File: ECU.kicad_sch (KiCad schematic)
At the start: 2 parts

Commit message: Create new top level
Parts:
- U?: value AEM_Infinity_5_Pin41-80 -> (none)
- U?: value AEM_Infinity_5_Pin1-40 -> (none)
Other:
- removed sheet Engine Overview
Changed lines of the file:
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@@
       (effects (font (size 1.27 1.27)) (justify left))
     )
-    (property "Value" "AEM_Infinity_5_Pin41-80" (id 1) (at 123.952 177.292 0)
+    (property "Value" "" (id 1) (at 123.952 177.292 0)
       (effects (font (size 1.27 1.27)) (justify left))
     )
@@
       (effects (font (size 1.27 1.27)) (justify left))
     )
-    (property "Value" "AEM_Infinity_5_Pin1-40" (id 1) (at 72.136 177.038 0)
+    (property "Value" "" (id 1) (at 72.136 177.038 0)
       (effects (font (size 1.27 1.27)) (justify left))
     )
@@
     )
   )
-  (sheet (at 246.38 25.4) (size 19.812 12.954) (fields_autoplaced)
-    (stroke (width 0.1524) (type solid) (color 0 0 0 0))
-    (fill (color 0 0 0 0.0000))
-    (property "Sheet name" "Engine Overview" (id 0) (at 246.38 24.6884 0)
-      (effects (font (size 1.27 1.27)) (justify left bottom))
-    )
-    (property "Sheet file" "Engine.kicad_sch" (id 1) (at 246.38 38.9386 0)
-      (effects (font (size 1.27 1.27)) (justify left top))
-    )
-  )

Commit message: HUGE TOP LEVEL
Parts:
- U?: value (none) -> AEM_Infinity_5_Pin41-80
- U?: value (none) -> AEM_Infinity_5_Pin1-40
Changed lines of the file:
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@@
       (effects (font (size 1.27 1.27)) (justify left))
     )
-    (property "Value" "" (id 1) (at 123.952 177.292 0)
+    (property "Value" "AEM_Infinity_5_Pin41-80" (id 1) (at 123.952 177.292 0)
       (effects (font (size 1.27 1.27)) (justify left))
     )
@@
       (effects (font (size 1.27 1.27)) (justify left))
     )
-    (property "Value" "" (id 1) (at 72.136 177.038 0)
+    (property "Value" "AEM_Infinity_5_Pin1-40" (id 1) (at 72.136 177.038 0)
       (effects (font (size 1.27 1.27)) (justify left))
     )

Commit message: Filled in Many Sheets
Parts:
- removed U?: AEM_Infinity_5_Pin41-80, symbol SCR23 Library:AEM_Infinity_5_Pin41-80
- removed U?: AEM_Infinity_5_Pin1-40, symbol SCR23 Library:AEM_Infinity_5_Pin1-40
- added U?: ECU, symbol Ty lib:ECU
- added U?: AEM_Infinity_5_Pin41-80, symbol SCR23 Library:AEM_Infinity_5_Pin41-80
- added U?: DTM_12P_BROWN_FEMALE, symbol SCR23 Library:DTM04-12pb
- added U?: DTM_12P_GRAY_FEMALE, symbol SCR23 Library:DTM04-12pb
- added U?: DTM_12P_BLACK_FEMALE, symbol SCR23 Library:DTM04-12pb
- added U?: DTM_12P_GREEN_FEMALE, symbol SCR23 Library:DTM04-12pb
- added U?: DT_12P_BLACK_FEMALE, symbol SCR23 Library:DTM04-12pb
- added U?: DT_12P_GREEN_FEMALE, symbol SCR23 Library:DTM04-12pb
- added U?: AEM_Infinity_5_Pin1-40, symbol SCR23 Library:AEM_Infinity_5_Pin1-40
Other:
- removed sheet Charging System
- removed sheet Coil Overview
- removed sheet DTM Dash
- removed sheet ECU Main Loom
- added sheet ECU Pinout (ECU_Pinout.kicad_sch)
- note added: "Black DTM 12P to FUSEBOX"
- note added: "ECU"
- note added: "ECU to COIL DRIVER"
- note added: "ECU to FUSEBOX"
- note added: "ECU to INJECTOR"
- note added: "GOES TO DASHBOARD"

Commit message: Getting Ready for CDR
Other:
- added sheet Coil Driver (Coil_Driver.kicad_sch)
- note added: "ECU to ENGINE"
- note removed: "ECU to COIL DRIVER"
- note removed: "ECU to INJECTOR"
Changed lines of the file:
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@@
     (effects (font (size 1.27 1.27)) (justify left bottom))
   )
-  (text "ECU to COIL DRIVER" (at 244.602 76.2 0)
+  (text "ECU to ENGINE" (at 244.602 76.2 0)
     (effects (font (size 1.27 1.27)) (justify left bottom))
   )
@@
     (effects (font (size 1.27 1.27)) (justify left bottom))
   )
-  (text "ECU to INJECTOR" (at 207.264 76.962 0)
+  (text "ECU to ENGINE" (at 207.264 76.962 0)
     (effects (font (size 1.27 1.27)) (justify left bottom))
   )
@@
     (property "Intersheet References" "${INTERSHEET_REFS}" (id 0) (at 192.4008 29.1545 0)
       (effects (font (size 0.889 0.889)) (justify left) hide)
+    )
+  )
+  (global_label "GND" (shape input) (at 233.426 45.974 180) (fields_autoplaced)
+    (effects (font (size 0.889 0.889)) (justify right))
+    (property "Intersheet References" "${INTERSHEET_REFS}" (id 0) (at 229.0276 45.9185 0)
+      (effects (font (size 0.889 0.889)) (justify right) hide)
     )
   )
@@
     )
   )
+  (global_label "11 - Coil 4" (shape input) (at 233.426 43.942 180) (fields_autoplaced)
+    (effects (font (size 0.889 0.889)) (justify right))
+    (property "Intersheet References" "${INTERSHEET_REFS}" (id 0) (at 223.4819 43.8865 0)
+      (effects (font (size 0.889 0.889)) (justify right) hide)
+    )
+  )
   (global_label "Injection 2 - 77" (shape input) (at 179.324 27.178 0) (fields_autoplaced)
     (effects (font (size 0.889 0.889)) (justify left))
@@
     (property "Intersheet References" "${INTERSHEET_REFS}" (id 0) (at 145.6648 53.2845 0)
       (effects (font (size 0.889 0.889)) (justify left) hide)
+    )
+  )
+  (global_label "12 - Coil 3" (shape input) (at 233.426 41.91 180) (fields_autoplaced)
+    (effects (font (size 0.889 0.889)) (justify right))
+    (property "Intersheet References" "${INTERSHEET_REFS}" (id 0) (at 223.4819 41.8545 0)
+      (effects (font (size 0.889 0.889)) (justify right) hide)
     )
   )
@@
     )
   )
+  (global_label "13 - Coil 2" (shape input) (at 233.426 39.878 180) (fields_autoplaced)
+    (effects (font (size 0.889 0.889)) (justify right))
+    (property "Intersheet References" "${INTERSHEET_REFS}" (id 0) (at 223.4819 39.8225 0)
+      (effects (font (size 0.889 0.889)) (justify right) hide)
+    )
+  )
   (global_label "13 - Coil 2" (shape input) (at 106.68 35.052 180) (fields_autoplaced)
     (effects (font (size 0.889 0.889)) (justify right))
@@
     )
   )
+  (global_label "14 - Coil 1" (shape input) (at 233.426 37.846 180) (fields_autoplaced)
+    (effects (font (size 0.889 0.889)) (justify right))
+    (property "Intersheet References" "${INTERSHEET_REFS}" (id 0) (at 223.4819 37.7905 0)
+      (effects (font (size 0.889 0.889)) (justify right) hide)
+    )
+  )
   (global_label "Ground - 33" (shape input) (at 127 35.052 0) (fields_autoplaced)
     (effects (font (size 0.889 0.889)) (justify left))
@@
       (effects (font (size 0.889 0.889)) (justify left) hide)
     )
+  )
+  (hierarchical_label "COIL_SGN_4" (shape input) (at 233.426 37.846 0)
+    (effects (font (size 1.27 1.27)) (justify left))
+  )
+  (hierarchical_label "COIL_4" (shape output) (at 261.366 37.846 0)
+    (effects (font (size 1.27 1.27)) (justify left))
+  )
+  (hierarchical_label "COIL_GND" (shape input) (at 233.426 45.974 0)
+    (effects (font (size 1.27 1.27)) (justify left))
+  )
+  (hierarchical_label "COIL_SGN_3" (shape input) (at 233.426 39.878 0)
+    (effects (font (size 1.27 1.27)) (justify left))
+  )
+  (hierarchical_label "COIL_SGN_2" (shape input) (at 233.426 41.91 0)
+    (effects (font (size 1.27 1.27)) (justify left))
+  )
+  (hierarchical_label "COIL_2" (shape output) (at 261.366 41.91 0)
+    (effects (font (size 1.27 1.27)) (justify left))
+  )
+  (hierarchical_label "COIL_1" (shape output) (at 261.366 43.942 0)
+    (effects (font (size 1.27 1.27)) (justify left))
+  )
+  (hierarchical_label "COIL_3" (shape output) (at 261.366 39.878 0)
+    (effects (font (size 1.27 1.27)) (justify left))
+  )
+  (hierarchical_label "COIL_SGN_1" (shape input) (at 233.426 43.942 0)
+    (effects (font (size 1.27 1.27)) (justify left))
   )
   (symbol (lib_id "Ty lib:ECU") (at 49.022 166.37 0) (unit 1)
@@
       (effects (font (size 1.27 1.27)) (justify left top))
     )
+  )
+  (sheet (at 233.426 36.322) (size 27.94 10.922) (fields_autoplaced)
+    (stroke (width 0.1524) (type solid) (color 0 0 0 0))
+    (fill (color 0 0 0 0.0000))
+    (property "Sheet name" "Coil Driver" (id 0) (at 233.426 35.6104 0)
+      (effects (font (size 1.27 1.27)) (justify left bottom))
+    )
+    (property "Sheet file" "Coil_Driver.kicad_sch" (id 1) (at 233.426 47.8286 0)
+      (effects (font (size 1.27 1.27)) (justify left top))
+    )

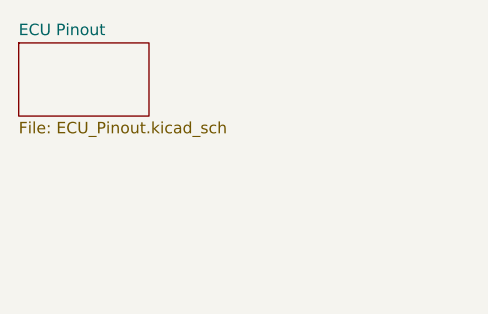
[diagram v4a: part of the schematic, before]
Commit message: Change to coil driver
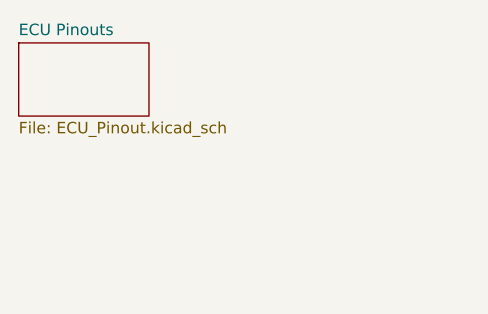
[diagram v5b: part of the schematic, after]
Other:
- sheet ECU Pinout renamed ECU Pinouts
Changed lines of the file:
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@@
     (stroke (width 0.1524) (type solid) (color 0 0 0 0))
     (fill (color 0 0 0 0.0000))
-    (property "Sheet name" "ECU Pinout" (id 0) (at 17.526 16.3064 0)
+    (property "Sheet name" "ECU Pinouts" (id 0) (at 17.526 16.3064 0)
       (effects (font (size 1.27 1.27)) (justify left bottom))
     )

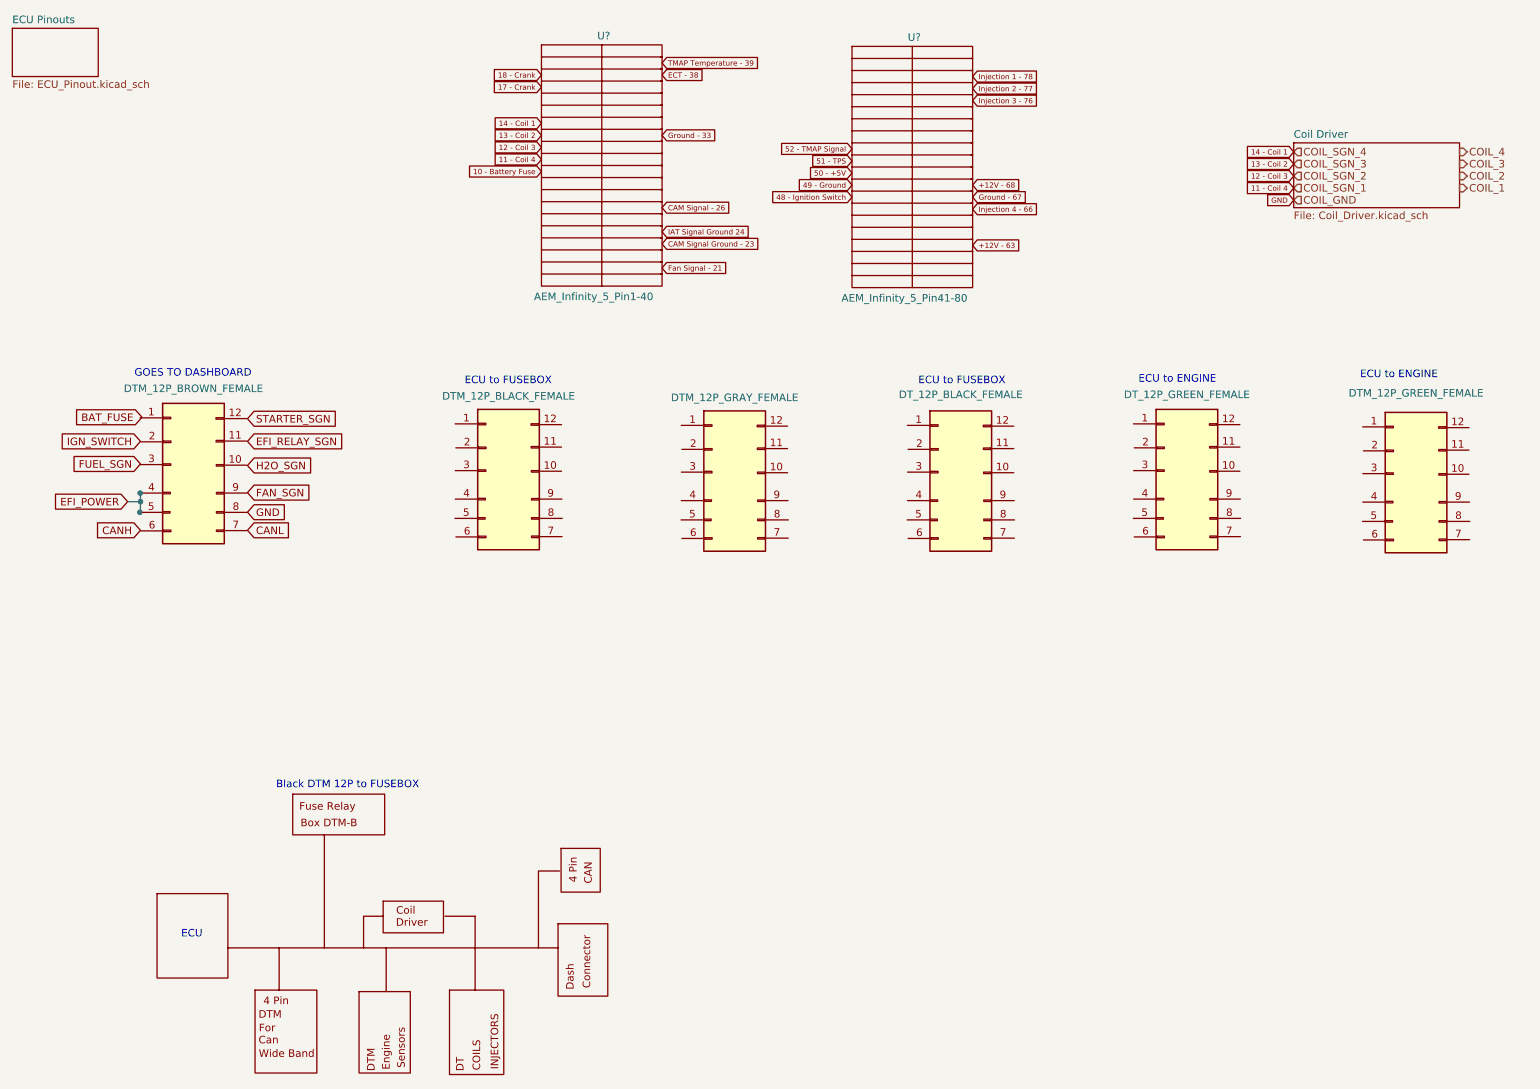
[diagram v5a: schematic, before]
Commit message: Updated Connectors
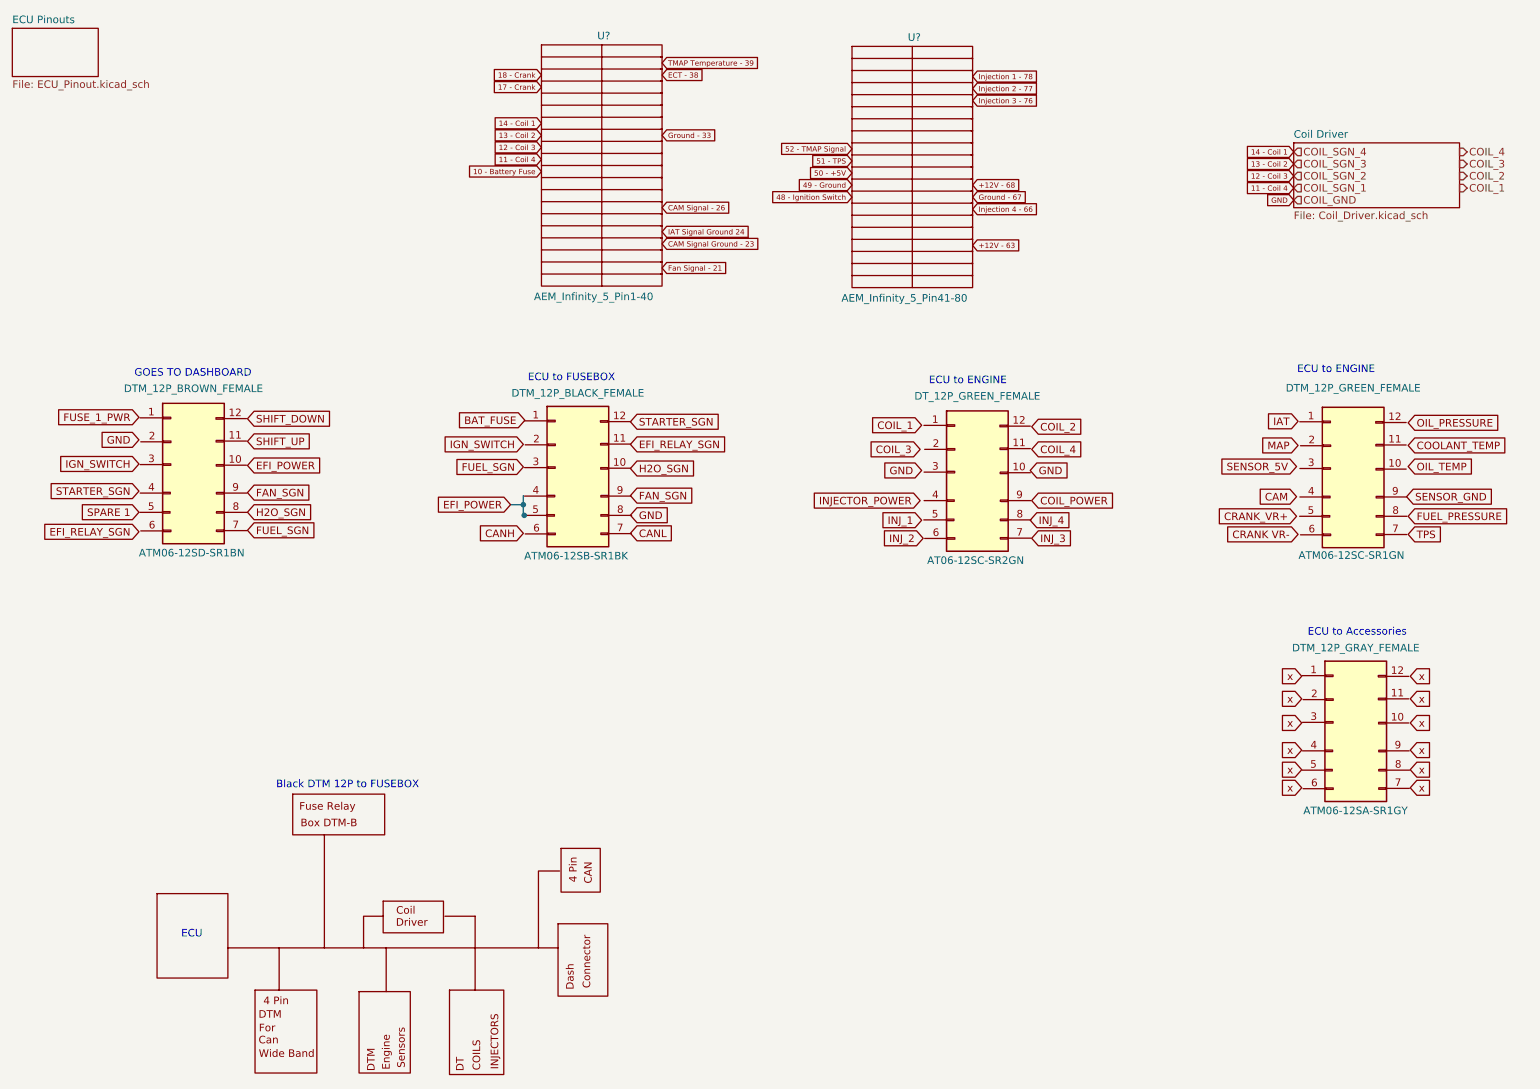
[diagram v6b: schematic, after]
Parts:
- removed U?: DT_12P_BLACK_FEMALE, symbol SCR23 Library:DTM04-12pb
- U?: Part # (none) -> ATM06-12SD-SR1BN
- U?: Part # (none) -> ATM06-12SA-SR1GY
- U?: Part # (none) -> ATM06-12SB-SR1BK
- U?: Part # (none) -> ATM06-12SC-SR1GN
- U?: Part # (none) -> AT06-12SC-SR2GN
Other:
- note added: "ECU to Accessories"

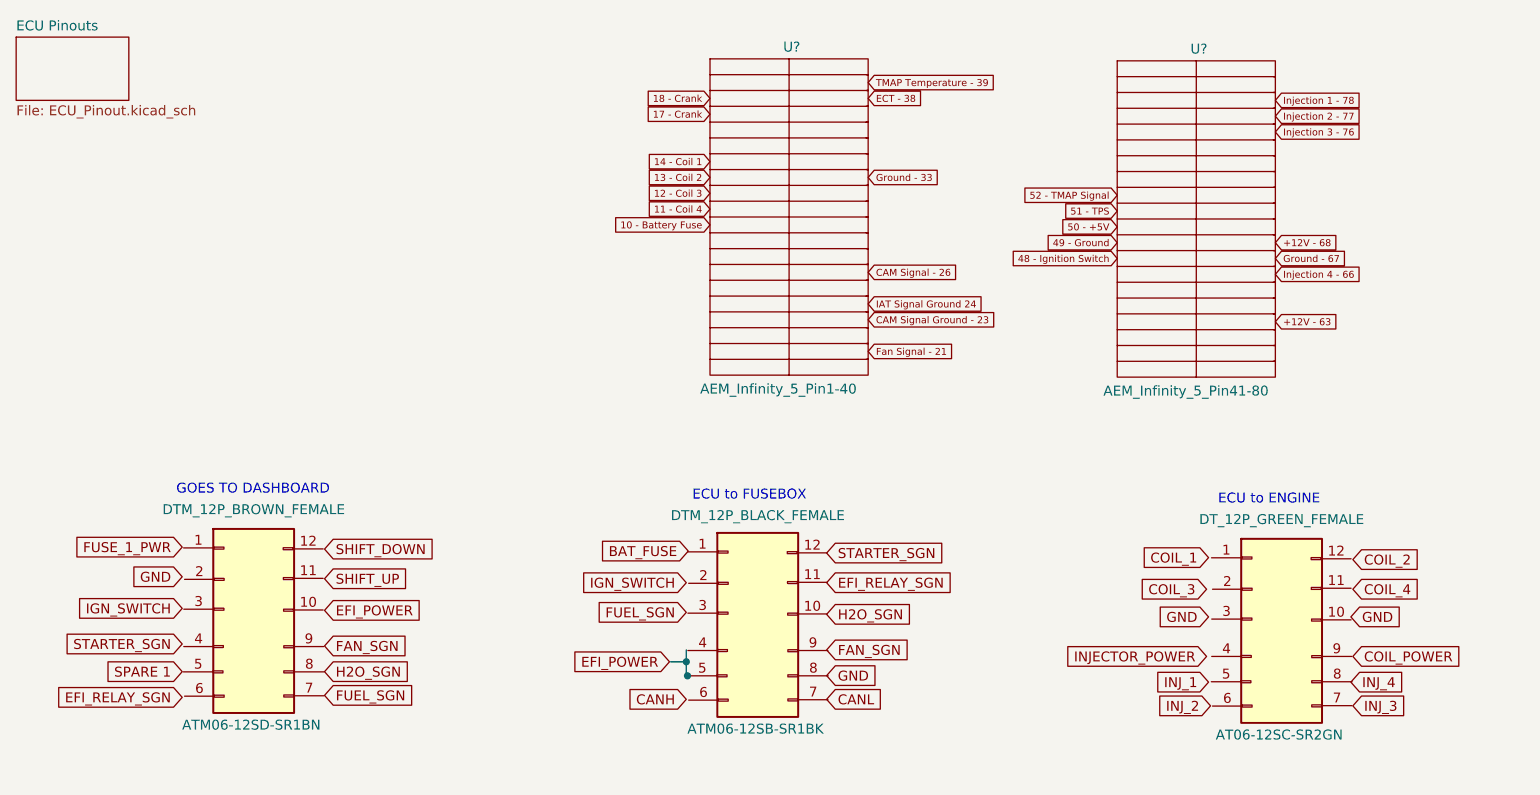
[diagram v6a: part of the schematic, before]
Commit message: Updated Connectors
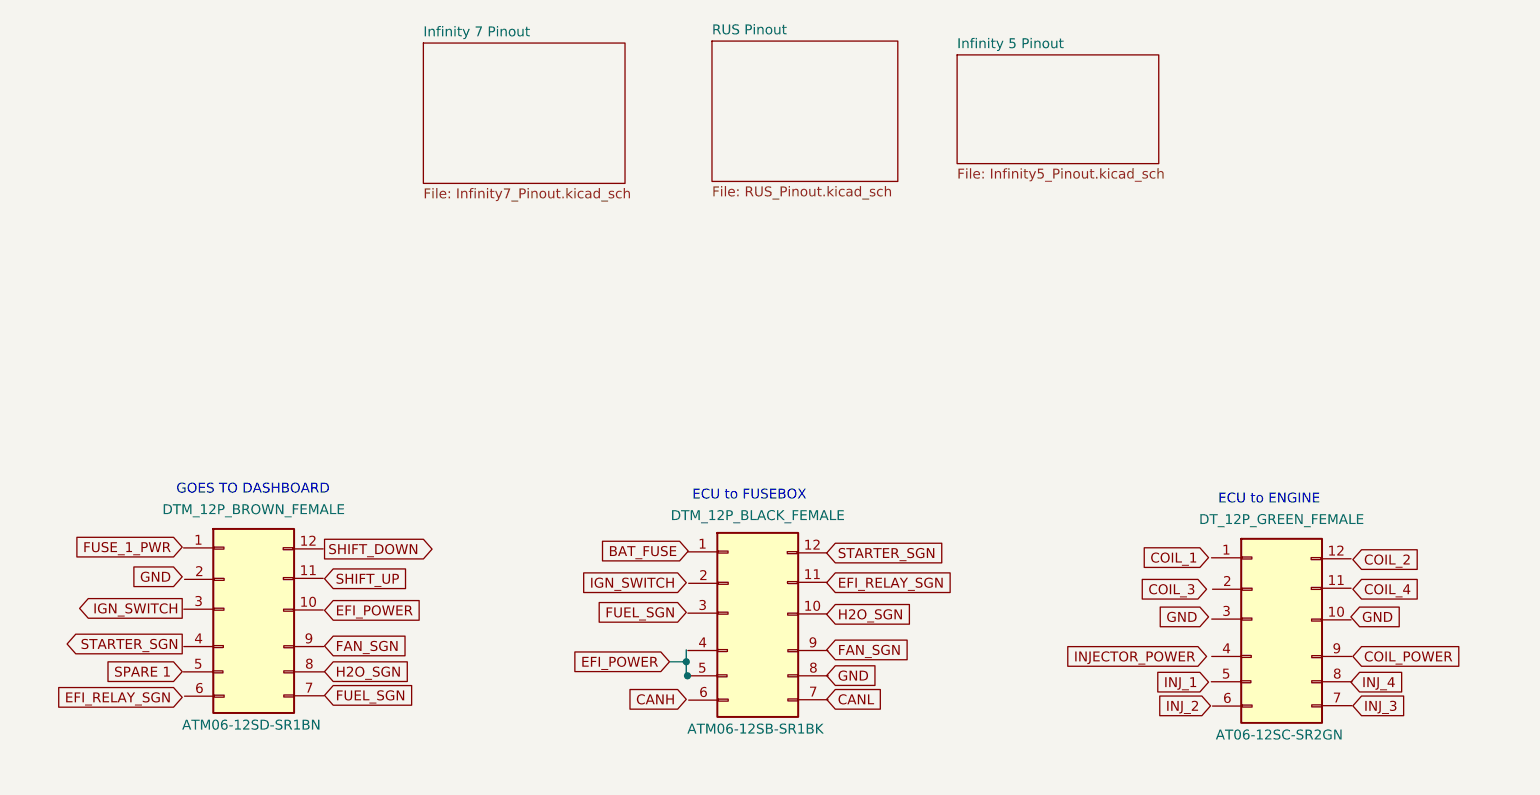
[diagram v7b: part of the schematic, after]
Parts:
- removed U?: AEM_Infinity_5_Pin41-80, symbol SCR23 Library:AEM_Infinity_5_Pin41-80
- removed U?: AEM_Infinity_5_Pin1-40, symbol SCR23 Library:AEM_Infinity_5_Pin1-40
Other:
- sheet ECU Pinouts renamed Infinity 7 Pinout
- added sheet Infinity 5 Pinout (Infinity5_Pinout.kicad_sch)
- added sheet RUS Pinout (RUS_Pinout.kicad_sch)
- sheet Infinity 7 Pinout: file ECU_Pinout.kicad_sch -> Infinity7_Pinout.kicad_sch
